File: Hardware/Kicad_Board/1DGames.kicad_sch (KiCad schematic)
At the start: 0 parts

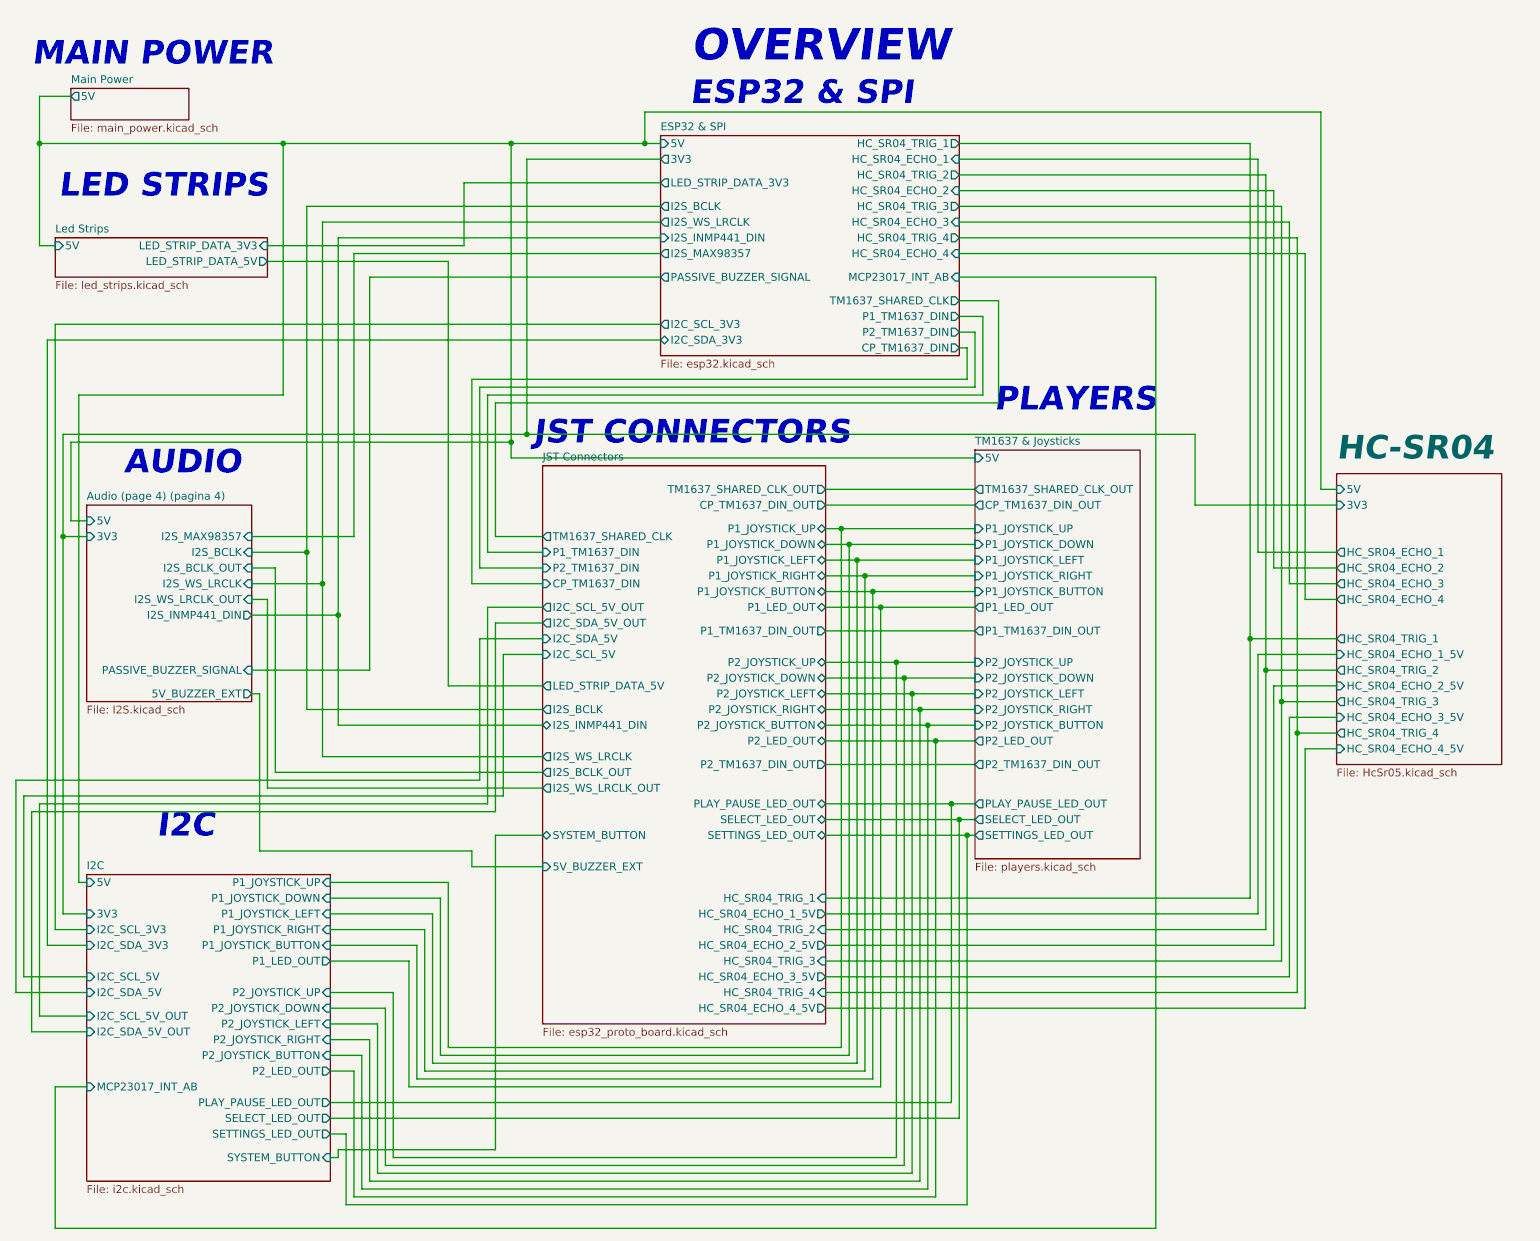
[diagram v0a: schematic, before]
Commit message: Added Kicad proto board
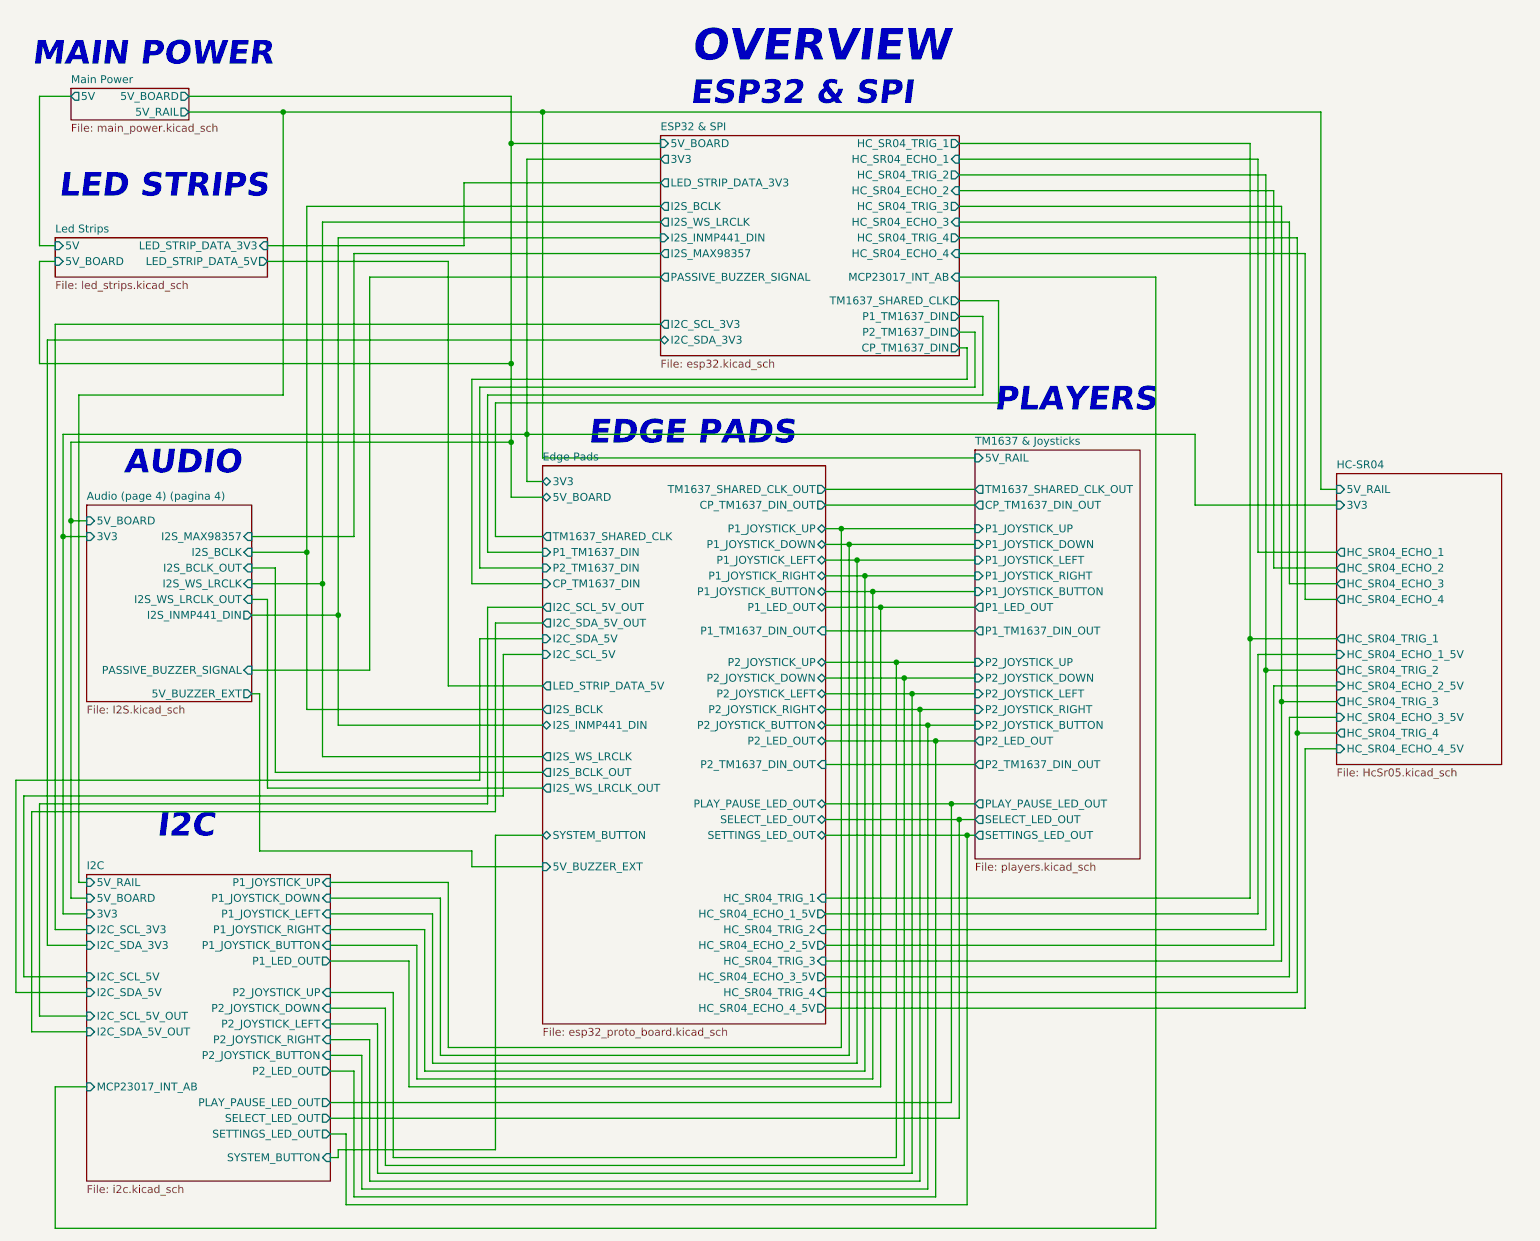
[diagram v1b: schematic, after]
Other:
- sheet JST Connectors renamed Edge Pads
- sheet Audio (page 4) (pagina 4) ports: added 5V_BOARD; removed 5V
- sheet ESP32 & SPI ports: added 5V_BOARD; removed 5V
- sheet Edge Pads ports: added 3V3, 5V_BOARD; removed none
- sheet HC-SR04 ports: added 5V_RAIL; removed 5V
- sheet I2C ports: added 5V_BOARD, 5V_RAIL; removed 5V
- sheet Led Strips ports: added 5V_BOARD; removed none
- sheet Main Power ports: added 5V_BOARD, 5V_RAIL; removed none
- sheet TM1637 & Joysticks ports: added 5V_RAIL; removed 5V
- note added: "EDGE PADS"
- note removed: "JST CONNECTORS"
